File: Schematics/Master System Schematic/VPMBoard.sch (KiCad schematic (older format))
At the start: 23 parts

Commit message: VPMBoard Annotations
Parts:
- gave numbers to parts that had none: 23
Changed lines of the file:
@@
 > If car is charging, GLV_PreBRB\n will be driven by ChargerSupply12V\n\n> If car is not charging, GLV_PreBRB \nwill be disconnected from the \ncharger supply
 $Comp
-L power:GND #PWR?
+L power:GND #PWR01
 U 1 1 5FCA9C4C
 P 2050 1900
-F 0 "#PWR?" H 2050 1650 50  0001 C CNN
+F 0 "#PWR01" H 2050 1650 50  0001 C CNN
 F 1 "GND" H 2055 1727 50  0000 C CNN
 F 2 "" H 2050 1900 50  0001 C CNN
@@
 	2050 2400 1950 2400
 $Comp
-L power:GND #PWR?
+L power:GND #PWR02
 U 1 1 5FCC4D73
 P 2050 2550
-F 0 "#PWR?" H 2050 2300 50  0001 C CNN
+F 0 "#PWR02" H 2050 2300 50  0001 C CNN
 F 1 "GND" H 2055 2377 50  0000 C CNN
 F 2 "" H 2050 2550 50  0001 C CNN
@@
 ThermEXIn12V
 $Comp
-L power:GND #PWR?
+L power:GND #PWR012
 U 1 1 5FD5EF12
 P 8950 1900
-F 0 "#PWR?" H 8950 1650 50  0001 C CNN
+F 0 "#PWR012" H 8950 1650 50  0001 C CNN
 F 1 "GND" H 8955 1727 50  0000 C CNN
 F 2 "" H 8950 1900 50  0001 C CNN
@@
 $EndComp
 $Comp
-L Connector:Conn_01x02_Female J?
+L Connector:Conn_01x02_Female J20
 U 1 1 5FC6E9A5
 P 9600 1650
-F 0 "J?" H 9492 1325 50  0000 C CNN
+F 0 "J20" H 9492 1325 50  0000 C CNN
 F 1 "Therm_PWR" H 9500 1400 50  0000 C CNN
 F 2 "" H 9600 1650 50  0001 C CNN
@@
 $EndComp
 $Comp
-L Connector:Conn_01x04_Female J?
+L Connector:Conn_01x04_Female J14
 U 1 1 5FBD5D22
 P 1450 6050
-F 0 "J?" H 1342 5625 50  0000 C CNN
+F 0 "J14" H 1342 5625 50  0000 C CNN
 F 1 "GLV_Signal" H 1342 5716 50  0000 C CNN
 F 2 "" H 1450 6050 50  0001 C CNN
@@
 $EndComp
 $Comp
-L Connector:Conn_01x04_Female J?
+L Connector:Conn_01x04_Female J1
 U 1 1 5FC1125D
 P 1450 5400
-F 0 "J?" H 1342 4975 50  0000 C CNN
+F 0 "J1" H 1342 4975 50  0000 C CNN
 F 1 "Charge_Signal" H 1342 5066 50  0000 C CNN
 F 2 "" H 1450 5400 50  0001 C CNN
@@
 $EndComp
 $Comp
-L Connector:Conn_01x04_Female J?
+L Connector:Conn_01x04_Female J15
 U 1 1 5FC7CBDE
 P 1450 6700
-F 0 "J?" H 1342 6275 50  0000 C CNN
+F 0 "J15" H 1342 6275 50  0000 C CNN
 F 1 "Therm_Signal" H 1342 6366 50  0000 C CNN
 F 2 "" H 1450 6700 50  0001 C CNN
@@
 NoConn ~ 1650 6500
 $Comp
-L Connector:Conn_01x06_Female J?
+L Connector:Conn_01x06_Female J19
 U 1 1 5FDAC8DD
 P 4450 5950
-F 0 "J?" H 4342 5425 50  0000 C CNN
+F 0 "J19" H 4342 5425 50  0000 C CNN
 F 1 "BMS_Signal" H 4342 5516 50  0000 C CNN
 F 2 "" H 4450 5950 50  0001 C CNN
@@
 CANS_Chrg
 $Comp
-L power:GND #PWR?
+L power:GND #PWR04
 U 1 1 5FC9259C
 P 2850 6900
-F 0 "#PWR?" H 2850 6650 50  0001 C CNN
+F 0 "#PWR04" H 2850 6650 50  0001 C CNN
 F 1 "GND" H 2855 6727 50  0000 C CNN
 F 2 "" H 2850 6900 50  0001 C CNN
@@
 	4000 3550 4600 3550
 $Comp
-L Device:Q_PMOS_GDS Q?
+L Device:Q_PMOS_GDS Q2
 U 1 1 5FCC6DCE
 P 5350 3450
-F 0 "Q?" V 5599 3450 50  0000 C CNN
+F 0 "Q2" V 5599 3450 50  0000 C CNN
 F 1 "SQP50P03-07" V 5690 3450 50  0000 C CNN
 F 2 "" H 5550 3550 50  0001 C CNN
@@
 	5650 3550 5550 3550
 $Comp
-L Device:Fuse F?
+L Device:Fuse F200
 U 1 1 5FC0FA27
 P 4950 3550
-F 0 "F?" V 5147 3550 50  0000 C CNN
+F 0 "F200" V 5147 3550 50  0000 C CNN
 F 1 "12A" V 5056 3550 50  0000 C CNN
 F 2 "" V 4880 3550 50  0001 C CNN
@@
 	8250 3150 8300 3150
 $Comp
-L Device:Fuse F?
+L Device:Fuse F202
 U 1 1 5FB0792D
 P 8450 3250
-F 0 "F?" V 8647 3250 50  0000 C CNN
+F 0 "F202" V 8647 3250 50  0000 C CNN
 F 1 "1A" V 8556 3250 50  0000 C CNN
 F 2 "" V 8380 3250 50  0001 C CNN
@@
 $EndComp
 $Comp
-L Device:Fuse F?
+L Device:Fuse F201
 U 1 1 5FB100A8
 P 8450 3150
-F 0 "F?" V 8647 3150 50  0000 C CNN
+F 0 "F201" V 8647 3150 50  0000 C CNN
 F 1 "1A" V 8556 3150 50  0000 C CNN
 F 2 "" V 8380 3150 50  0001 C CNN
@@
 $EndComp
 $Comp
-L power:GND #PWR?
+L power:GND #PWR013
 U 1 1 5FCBC47D
 P 8950 3500
-F 0 "#PWR?" H 8950 3250 50  0001 C CNN
+F 0 "#PWR013" H 8950 3250 50  0001 C CNN
 F 1 "GND" H 8955 3327 50  0000 C CNN
 F 2 "" H 8950 3500 50  0001 C CNN
@@
 	7100 1550 7100 3250
 $Comp
-L Device:Q_PMOS_GDS Q?
+L Device:Q_PMOS_GDS Q6
 U 1 1 5FD075B5
 P 7450 3150
-F 0 "Q?" V 7699 3150 50  0000 C CNN
+F 0 "Q6" V 7699 3150 50  0000 C CNN
 F 1 "SQP50P03-07" V 7790 3150 50  0000 C CNN
 F 2 "" H 7650 3250 50  0001 C CNN
@@
 $EndComp
 $Comp
-L power:GND #PWR?
+L power:GND #PWR011
 U 1 1 5FD1386A
 P 8100 2800
-F 0 "#PWR?" H 8100 2550 50  0001 C CNN
+F 0 "#PWR011" H 8100 2550 50  0001 C CNN
 F 1 "GND" H 8105 2627 50  0000 C CNN
 F 2 "" H 8100 2800 50  0001 C CNN
@@
 	7450 2450 7450 2750
 $Comp
-L Device:R R?
+L Device:R R13
 U 1 1 5FD172BE
 P 7450 2300
-F 0 "R?" H 7520 2346 50  0000 L CNN
+F 0 "R13" H 7520 2346 50  0000 L CNN
 F 1 "100K" H 7520 2255 50  0000 L CNN
 F 2 "" V 7380 2300 50  0001 C CNN
@@
 $EndComp
 $Comp
-L power:+12V #PWR?
+L power:+12V #PWR05
 U 1 1 5FD2774A
 P 4600 3450
-F 0 "#PWR?" H 4600 3300 50  0001 C CNN
+F 0 "#PWR05" H 4600 3300 50  0001 C CNN
 F 1 "+12V" H 4615 3623 50  0000 C CNN
 F 2 "" H 4600 3450 50  0001 C CNN
@@
 	4600 3550 4800 3550
 $Comp
-L power:+12V #PWR?
+L power:+12V #PWR010
 U 1 1 5FD37608
 P 7450 2150
-F 0 "#PWR?" H 7450 2000 50  0001 C CNN
+F 0 "#PWR010" H 7450 2000 50  0001 C CNN
 F 1 "+12V" H 7465 2323 50  0000 C CNN
 F 2 "" H 7450 2150 50  0001 C CNN
@@
 GLV_BMSContainer\n
 $Comp
-L Transistor_FET:2N7002 Q?
+L Transistor_FET:2N7002 Q3
 U 1 1 5FCB5015
 P 5750 3000
-F 0 "Q?" V 5999 3000 50  0000 C CNN
+F 0 "Q3" V 5999 3000 50  0000 C CNN
 F 1 "2N7002" V 6090 3000 50  0000 C CNN
 F 2 "Package_TO_SOT_SMD:SOT-23" H 5950 2925 50  0001 L CIN
@@
 	4000 1550 6550 1550
 $Comp
-L Transistor_FET:2N7002 Q?
+L Transistor_FET:2N7002 Q4
 U 1 1 5FCCB41E
 P 6150 3000
-F 0 "Q?" V 6399 3000 50  0000 C CNN
+F 0 "Q4" V 6399 3000 50  0000 C CNN
 F 1 "2N7002" V 6490 3000 50  0000 C CNN
 F 2 "Package_TO_SOT_SMD:SOT-23" H 6350 2925 50  0001 L CIN
@@
 $EndComp
 $Comp
-L power:GND #PWR?
+L power:GND #PWR08
 U 1 1 5FCCC1B3
 P 6450 3200
-F 0 "#PWR?" H 6450 2950 50  0001 C CNN
+F 0 "#PWR08" H 6450 2950 50  0001 C CNN
 F 1 "GND" H 6455 3027 50  0000 C CNN
 F 2 "" H 6450 3200 50  0001 C CNN
@@
 	5350 3100 5350 3250
 $Comp
-L Device:R R?
+L Device:R R11
 U 1 1 5FCCFBA3
 P 5350 2850
-F 0 "R?" H 5420 2896 50  0000 L CNN
+F 0 "R11" H 5420 2896 50  0000 L CNN
 F 1 "100K" H 5420 2805 50  0000 L CNN
 F 2 "" V 5280 2850 50  0001 C CNN
@@
 $EndComp
 $Comp
-L power:+12V #PWR?
+L power:+12V #PWR06
 U 1 1 5FCD0144
 P 5350 2700
-F 0 "#PWR?" H 5350 2550 50  0001 C CNN
+F 0 "#PWR06" H 5350 2550 50  0001 C CNN
 F 1 "+12V" H 5365 2873 50  0000 C CNN
 F 2 "" H 5350 2700 50  0001 C CNN
@@
 Connection ~ 5750 1650
 $Comp
-L Transistor_FET:2N7002 Q?
+L Transistor_FET:2N7002 Q5
 U 1 1 5FCD3A37
 P 6550 2350
-F 0 "Q?" V 6799 2350 50  0000 C CNN
+F 0 "Q5" V 6799 2350 50  0000 C CNN
 F 1 "2N7002" V 6890 2350 50  0000 C CNN
 F 2 "Package_TO_SOT_SMD:SOT-23" H 6750 2275 50  0001 L CIN
@@
 $EndComp
 $Comp
-L power:GND #PWR?
+L power:GND #PWR09
 U 1 1 5FCD73FE
 P 6850 2550
-F 0 "#PWR?" H 6850 2300 50  0001 C CNN
+F 0 "#PWR09" H 6850 2300 50  0001 C CNN
 F 1 "GND" H 6855 2377 50  0000 C CNN
 F 2 "" H 6850 2550 50  0001 C CNN
@@
 	6550 1550 7100 1550
 $Comp
-L Device:R R?
+L Device:R R12
 U 1 1 5FCDD1F1
 P 6150 2150
-F 0 "R?" H 6220 2196 50  0000 L CNN
+F 0 "R12" H 6220 2196 50  0000 L CNN
 F 1 "100K" H 6220 2105 50  0000 L CNN
 F 2 "" V 6080 2150 50  0001 C CNN
@@
 $EndComp
 $Comp
-L power:+12V #PWR?
+L power:+12V #PWR07
 U 1 1 5FCDD6C3
 P 6150 2000
-F 0 "#PWR?" H 6150 1850 50  0001 C CNN
+F 0 "#PWR07" H 6150 1850 50  0001 C CNN
 F 1 "+12V" H 6165 2173 50  0000 C CNN
 F 2 "" H 6150 2000 50  0001 C CNN
@@
 	5750 1650 7800 1650
 $Comp
-L Transistor_FET:2N7002 Q?
+L Transistor_FET:2N7002 Q7
 U 1 1 5FCE3DFD
 P 7800 2650
-F 0 "Q?" V 8049 2650 50  0000 C CNN
+F 0 "Q7" V 8049 2650 50  0000 C CNN
 F 1 "2N7002" V 8140 2650 50  0000 C CNN
 F 2 "Package_TO_SOT_SMD:SOT-23" H 8000 2575 50  0001 L CIN
@@
 	2700 2550 2700 2400
 $Comp
-L power:GND #PWR?
+L power:GND #PWR03
 U 1 1 5FCAF3C3
 P 2700 2550
-F 0 "#PWR?" H 2700 2300 50  0001 C CNN
+F 0 "#PWR03" H 2700 2300 50  0001 C CNN
 F 1 "GND" H 2705 2377 50  0000 C CNN
 F 2 "" H 2700 2550 50  0001 C CNN
@@
 	3650 2300 3700 2300
 $Comp
-L Device:Q_NMOS_GDS Q?
+L Device:Q_NMOS_GDS Q1
 U 1 1 5FCA0094
 P 3900 2300
-F 0 "Q?" H 4104 2254 50  0000 L CNN
+F 0 "Q1" H 4104 2254 50  0000 L CNN
 F 1 "FDP3632" H 4104 2345 50  0000 L CNN
 F 2 "" H 4100 2400 50  0001 C CNN
@@
 $EndComp
 $Comp
-L Power_Management:LTC4357MS8 U?
+L Power_Management:LTC4357MS8 U5
 U 1 1 5FC9E54A
 P 3250 2400
-F 0 "U?" V 2850 1950 50  0000 C CNN
+F 0 "U5" V 2850 1950 50  0000 C CNN
 F 1 "LTC4357MS8" V 2950 2050 50  0000 C CNN
 F 2 "Package_SO:MSOP-8_3x3mm_P0.65mm" H 3500 2250 50  0001 L CNN
@@
 GLV_PreBRB
 $Comp
-L NER:2-Pos_Generic J?
+L NER:2-Pos_Generic J16
 U 1 1 60052B8B
 P 1500 3450
-F 0 "J?" H 1500 3575 50  0000 C CNN
+F 0 "J16" H 1500 3575 50  0000 C CNN
 F 1 "PumpIO" H 1500 3484 50  0000 C CNN
 F 2 "" H 1500 3450 50  0001 C CNN
@@
 	1250 3650 1200 3650
 $Comp
-L NER:3-Pos_Generic J?
+L NER:3-Pos_Generic J17
 U 1 1 60084A61
 P 1700 1450
-F 0 "J?" H 1700 1575 50  0000 C CNN
+F 0 "J17" H 1700 1575 50  0000 C CNN
 F 1 "GLV/Charge_PWR" H 1700 1484 50  0000 C CNN
 F 2 "" H 1700 1450 50  0001 C CNN
@@
 	1450 1550 1400 1550
 $Comp
-L NER:1-Pos_Generic J?
+L NER:1-Pos_Generic J18
 U 1 1 600B3510
 P 1700 2300
-F 0 "J?" H 1700 2425 50  0000 C CNN
+F 0 "J18" H 1700 2425 50  0000 C CNN
 F 1 "GND_QC" H 1700 2334 50  0000 C CNN
 F 2 "" H 1700 2300 50  0001 C CNN
@@
 	1450 1750 1400 1750
 $Comp
-L NER:3-Pos_Generic J?
+L NER:3-Pos_Generic J21
 U 1 1 6116408D
 P 9650 3050
-F 0 "J?" H 9650 3175 50  0000 C CNN
+F 0 "J21" H 9650 3175 50  0000 C CNN
 F 1 "BMS_PWR" H 9650 3084 50  0000 C CNN
 F 2 "" H 9650 3050 50  0001 C CNN

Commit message: Added/Fixed Sheet Connections Within BMS Container
> Added hierarchical labels for each input on the VPM and connected them to hierarchical labels and the BMS within the BMS container.
> Added CANS(Charger) hierarchical label coming out of the BMS container sheet and connected it to the charger CAN bus line.

BMS Container Version 8.1
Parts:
- removed J1: Charge_Signal, symbol Connector:Conn_01x04_Female
- removed J14: GLV_Signal, symbol Connector:Conn_01x04_Female
- removed J15: Therm_Signal, symbol Connector:Conn_01x04_Female
- removed J19: BMS_Signal, symbol Connector:Conn_01x06_Female
- removed J20: Therm_PWR, symbol Connector:Conn_01x02_Female
- added J1: Charge_Signal, symbol NER:4-Pos_Generic
- added J14: Main_Signal, symbol NER:4-Pos_Generic
- added J15: Therm_Signal, symbol NER:4-Pos_Generic
- added J19: BMS_Signal, symbol NER:6-Pos_Generic
- added J20: ThermEX_PWR, symbol NER:2-Pos_Generic
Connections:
- net labels added: BMS_Fault, CANH_BMS, CANH_Chrg, CANH_Main, CANH_Thrm, CANL_BMS, CANL_Chrg, CANL_Main, CANL_Thrm, CANS_BMS, CANS_Chrg, CANS_Main, CANS_Thrm, Charge_Safety, ChargerSafety, MP_EN, ThermEX_GND, ThermEX_PWR
- net labels removed: ???
- no-connect marks 2 -> 4
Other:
- note added: "ThermEX_PWR\n"
- note removed: "ThermEXIn12V"
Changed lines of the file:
@@
 EESchema Schematic File Version 4
-LIBS:Master System Schematic-cache
 EELAYER 30 0
 EELAYER END
@@
 	8950 1900 8950 1750
 Connection ~ 8250 1650
-Text Notes 9350 1650 2    50   ~ 0
-ThermEXIn12V
 $Comp
 L power:GND #PWR012
@@
 	-1   0    0    -1
 $EndComp
-$Comp
-L Connector:Conn_01x02_Female J20
-U 1 1 5FC6E9A5
-P 9600 1650
-F 0 "J20" H 9492 1325 50  0000 C CNN
-F 1 "Therm_PWR" H 9500 1400 50  0000 C CNN
-F 2 "" H 9600 1650 50  0001 C CNN
-F 3 "~" H 9600 1650 50  0001 C CNN
-	1    9600 1650
-	1    0    0    -1
-$EndComp
-$Comp
-L Connector:Conn_01x04_Female J14
-U 1 1 5FBD5D22
-P 1450 6050
-F 0 "J14" H 1342 5625 50  0000 C CNN
-F 1 "GLV_Signal" H 1342 5716 50  0000 C CNN
-F 2 "" H 1450 6050 50  0001 C CNN
-F 3 "~" H 1450 6050 50  0001 C CNN
-	1    1450 6050
-	-1   0    0    1
-$EndComp
-$Comp
-L Connector:Conn_01x04_Female J1
-U 1 1 5FC1125D
-P 1450 5400
-F 0 "J1" H 1342 4975 50  0000 C CNN
-F 1 "Charge_Signal" H 1342 5066 50  0000 C CNN
-F 2 "" H 1450 5400 50  0001 C CNN
-F 3 "~" H 1450 5400 50  0001 C CNN
-	1    1450 5400
-	-1   0    0    1
-$EndComp
-$Comp
-L Connector:Conn_01x04_Female J15
-U 1 1 5FC7CBDE
-P 1450 6700
-F 0 "J15" H 1342 6275 50  0000 C CNN
-F 1 "Therm_Signal" H 1342 6366 50  0000 C CNN
-F 2 "" H 1450 6700 50  0001 C CNN
-F 3 "~" H 1450 6700 50  0001 C CNN
-	1    1450 6700
-	-1   0    0    1
-$EndComp
 NoConn ~ 1650 6500
-$Comp
-L Connector:Conn_01x06_Female J19
-U 1 1 5FDAC8DD
-P 4450 5950
-F 0 "J19" H 4342 5425 50  0000 C CNN
-F 1 "BMS_Signal" H 4342 5516 50  0000 C CNN
-F 2 "" H 4450 5950 50  0001 C CNN
-F 3 "~" H 4450 5950 50  0001 C CNN
-	1    4450 5950
-	1    0    0    1
-$EndComp
 Wire Wire Line
 	1650 5950 3050 5950
@@
 F 3 "" H 1700 2300 50  0001 C CNN
 	1    1700 2300
-	1    0    0    -1
+	-1   0    0    -1
 $EndComp
 Text HLabel 1400 1750 0    50   UnSpc ~ 0
@@
 PWR_Ready
 Text HLabel 9950 3350 2    50   Output ~ 0
-???
+BMS_GND
 Wire Wire Line
 	9950 3350 9900 3350
@@
 Wire Wire Line
 	9950 3150 9900 3150
+$Comp
+L NER:2-Pos_Generic J20
+U 1 1 600B417F
+P 9650 1550
+F 0 "J20" H 9650 1675 50  0000 C CNN
+F 1 "ThermEX_PWR" H 9650 1584 50  0000 C CNN
+F 2 "" H 9650 1550 50  0001 C CNN
+F 3 "" H 9650 1550 50  0001 C CNN
+	1    9650 1550
+	1    0    0    -1
+$EndComp
+Text HLabel 9900 1750 2    50   Output ~ 0
+ThermEX_GND
+Text HLabel 9900 1650 2    50   Output ~ 0
+ThermEX_PWR
+Text Notes 9350 1650 2    50   ~ 0
+ThermEX_PWR\n
+$Comp
+L NER:4-Pos_Generic J14
+U 1 1 600E1D3A
+P 1400 5750
+F 0 "J14" H 1400 5875 50  0000 C CNN
+F 1 "Main_Signal" H 1400 5784 50  0000 C CNN
+F 2 "" H 1400 5750 50  0001 C CNN
+F 3 "" H 1400 5750 50  0001 C CNN
+	1    1400 5750
+	-1   0    0    -1
+$EndComp
+$Comp
+L NER:4-Pos_Generic J15
+U 1 1 600E4AAA
+P 1400 6400
+F 0 "J15" H 1400 6525 50  0000 C CNN
+F 1 "Therm_Signal" H 1400 6434 50  0000 C CNN
+F 2 "" H 1400 6400 50  0001 C CNN
+F 3 "" H 1400 6400 50  0001 C CNN
+	1    1400 6400
+	-1   0    0    -1
+$EndComp
+NoConn ~ 1150 6500
+Text HLabel 1150 5500 0    50   Input ~ 0
+CANS_Chrg
+Text HLabel 1150 5400 0    50   Input ~ 0
+CANL_Chrg
+Text HLabel 1150 5300 0    50   Input ~ 0
+CANH_Chrg
+Text HLabel 1150 5200 0    50   Input ~ 0
+ChargerSafety
+Text HLabel 1150 6150 0    50   Input ~ 0
+CANS_Main
+Text HLabel 1150 6050 0    50   Input ~ 0
+CANL_Main
+Text HLabel 1150 5950 0    50   Input ~ 0
+CANH_Main
+Text HLabel 1150 5850 0    50   Input ~ 0
+BMS_Fault
+Text HLabel 1150 6800 0    50   Input ~ 0
+CANS_Thrm
+Text HLabel 1150 6600 0    50   Input ~ 0
+CANH_Thrm
+Text HLabel 1150 6700 0    50   Input ~ 0
+CANL_Thrm
+$Comp
+L NER:6-Pos_Generic J19
+U 1 1 600F4343
+P 4500 5550
+F 0 "J19" H 4500 5675 50  0000 C CNN
+F 1 "BMS_Signal" H 4500 5584 50  0000 C CNN
+F 2 "" H 4500 5550 50  0001 C CNN
+F 3 "" H 4500 5550 50  0001 C CNN
+	1    4500 5550
+	1    0    0    -1
+$EndComp
+$Comp
+L NER:4-Pos_Generic J1
+U 1 1 600D5093
+P 1400 5100
+F 0 "J1" H 1400 5225 50  0000 C CNN
+F 1 "Charge_Signal" H 1400 5134 50  0000 C CNN
+F 2 "" H 1400 5100 50  0001 C CNN
+F 3 "" H 1400 5100 50  0001 C CNN
+	1    1400 5100
+	-1   0    0    -1
+$EndComp
+NoConn ~ 4750 5650
+Text HLabel 4750 5750 2    50   Input ~ 0
+Charge_Safety
+Text HLabel 4750 5850 2    50   Input ~ 0
+MP_EN
+Text HLabel 4750 5950 2    50   Input ~ 0
+CANH_BMS
+Text HLabel 4750 6050 2    50   Input ~ 0
+CANL_BMS
+Text HLabel 4750 6150 2    50   Input ~ 0
+CANS_BMS
 $EndSCHEMATC

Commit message: Moved Pump power fuse to branching point
moved to GLVMS
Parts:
- removed F200: 12A, symbol Device:Fuse
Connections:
- net +12V: now also Q2.3 (S)
- new net: J1.1, J19.2
- new net: J1.2, J14.2, J15.2, J19.4
- new net: J1.3, J14.3, J15.3, J19.5
- new net: J14.1, J19.3
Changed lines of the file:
@@
 	1650 5850 4250 5850
 NoConn ~ 4250 5650
-Wire Wire Line
-	5100 3550 5150 3550
-Wire Wire Line
-	4000 3550 4600 3550
 $Comp
 L Device:Q_PMOS_GDS Q2
@@
 Wire Wire Line
 	5650 3550 5550 3550
-$Comp
-L Device:Fuse F200
-U 1 1 5FC0FA27
-P 4950 3550
-F 0 "F200" V 5147 3550 50  0000 C CNN
-F 1 "12A" V 5056 3550 50  0000 C CNN
-F 2 "" V 4880 3550 50  0001 C CNN
-F 3 "~" H 4950 3550 50  0001 C CNN
-	1    4950 3550
-	0    -1   -1   0
-$EndComp
 Wire Wire Line
 	8250 1650 8250 3150
@@
 	1    0    0    -1
 $EndComp
-Wire Wire Line
-	4600 3450 4600 3550
-Connection ~ 4600 3550
-Wire Wire Line
-	4600 3550 4800 3550
 $Comp
 L power:+12V #PWR010
@@
 Text HLabel 4750 6150 2    50   Input ~ 0
 CANS_BMS
+Wire Wire Line
+	4000 3550 4600 3550
+Wire Wire Line
+	4600 3450 4600 3550
+Connection ~ 4600 3550
+Wire Wire Line
+	4600 3550 5150 3550
 $EndSCHEMATC

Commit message: Annotation and Revision numbers
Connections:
- new net: J1.1, J19.2
- new net: J1.2, J14.2, J15.2, J19.4
- new net: J1.3, J14.3, J15.3, J19.5
- new net: J14.1, J19.3
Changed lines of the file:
@@
 Sheet 22 23
 Title "Vehicle Power Management Board"
-Date "2020-12-05"
-Rev "4.1"
+Date "2021-01-30"
+Rev "4.2"
 Comp "Northeastern Electric Racing"
 Comment1 "https://github.com/Northeastern-Electric-Racing/NER"

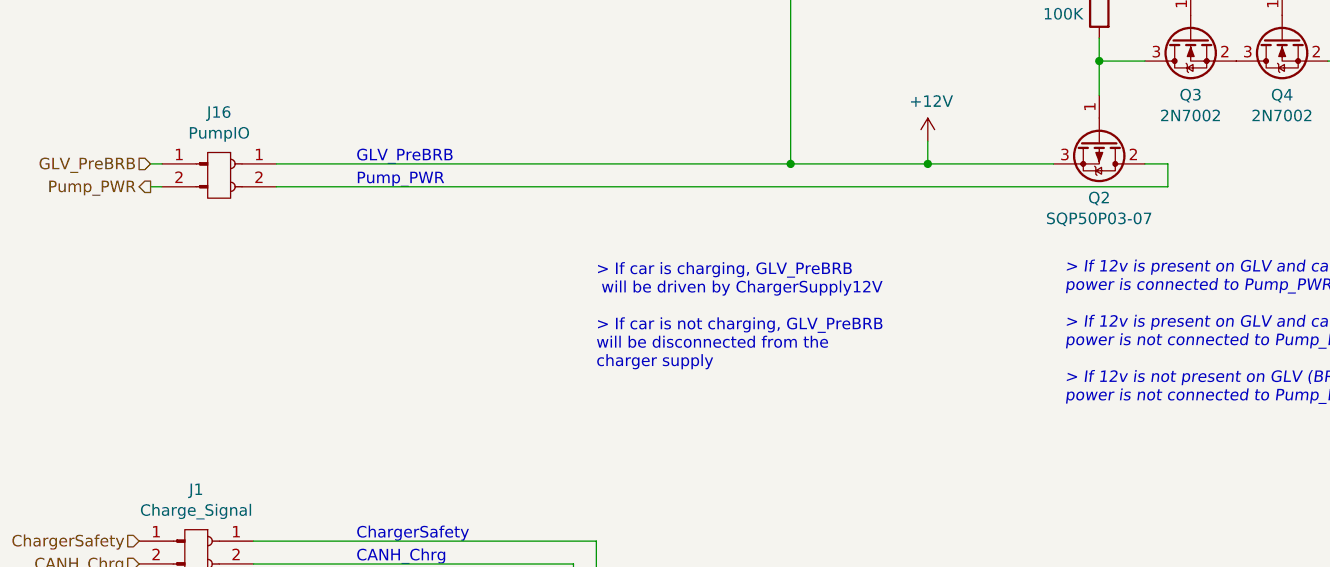
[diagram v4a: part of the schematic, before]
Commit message: VPM Board Flyback Diode
> Added MBRD5100 diode for protection against voltage spikes when switching the motor.
> Added note explaining this ^

VPM Board Version 4.3
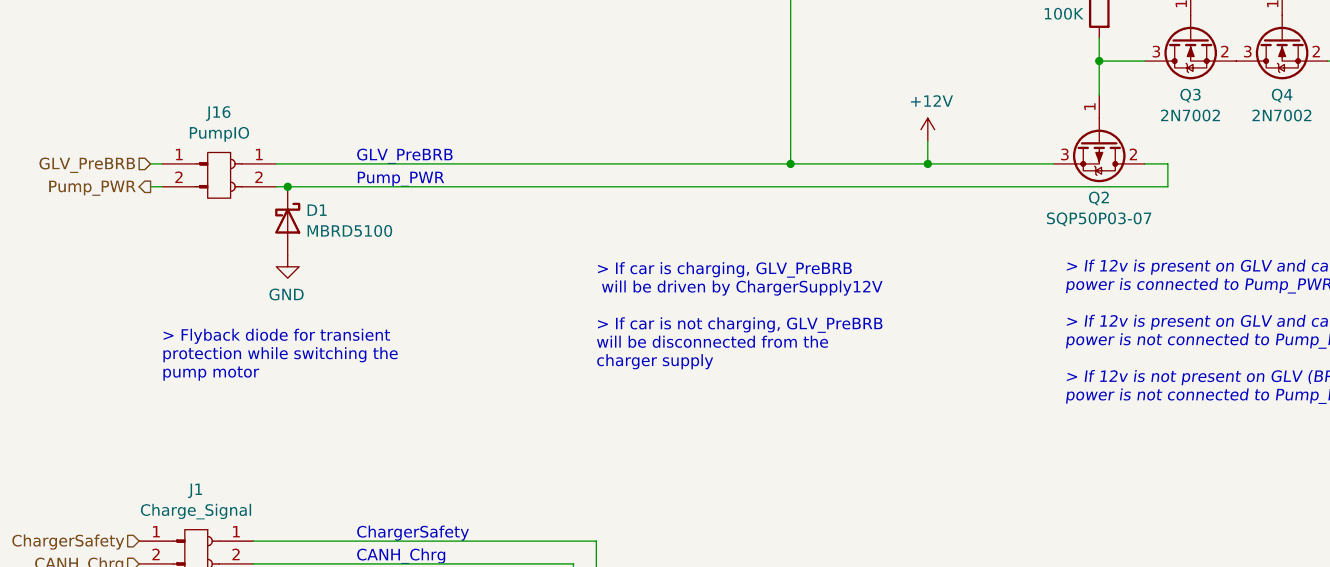
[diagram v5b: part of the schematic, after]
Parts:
- added D1: MBRD5100, Diode_SMD:D_SOD-123, symbol Diode:MBR0520
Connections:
- net GND: now also D1.2 (A)
- net at J16.2, Q2.2 (D): now also D1.1 (K)
- new net: J1.1, J19.2
- new net: J1.2, J14.2, J15.2, J19.4
- new net: J1.3, J14.3, J15.3, J19.5
- new net: J14.1, J19.3
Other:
- note added: "> Flyback diode for transient\nprotection while switching the \npump motor"
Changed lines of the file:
@@
 Sheet 22 23
 Title "Vehicle Power Management Board"
-Date "2021-01-30"
-Rev "4.2"
+Date "2021-02-11"
+Rev "4.3"
 Comp "Northeastern Electric Racing"
 Comment1 "https://github.com/Northeastern-Electric-Racing/NER"
@@
 	1750 3550 4000 3550
 Wire Wire Line
-	1750 3650 5650 3650
+	1750 3650 1800 3650
 Wire Wire Line
 	1250 3550 1200 3550
@@
 Wire Wire Line
 	4600 3550 5150 3550
+$Comp
+L Diode:MBR0520 D1
+U 1 1 602AC2AA
+P 1800 3800
+F 0 "D1" V 1754 3880 50  0000 L CNN
+F 1 "MBRD5100" V 1845 3880 50  0000 L CNN
+F 2 "Diode_SMD:D_SOD-123" H 1800 3625 50  0001 C CNN
+F 3 "http://www.mccsemi.com/up_pdf/MBR0520~MBR0580(SOD123).pdf" H 1800 3800 50  0001 C CNN
+	1    1800 3800
+	0    1    1    0
+$EndComp
+$Comp
+L power:GND #PWR014
+U 1 1 602ADBC9
+P 1800 3950
+F 0 "#PWR014" H 1800 3700 50  0001 C CNN
+F 1 "GND" H 1805 3777 50  0000 C CNN
+F 2 "" H 1800 3950 50  0001 C CNN
+F 3 "" H 1800 3950 50  0001 C CNN
+	1    1800 3950
+	-1   0    0    -1
+$EndComp
+Text Notes 1250 4500 0    50   ~ 0
+> Flyback diode for transient\nprotection while switching the \npump motor
+Connection ~ 1800 3650
+Wire Wire Line
+	1800 3650 5650 3650
 $EndSCHEMATC

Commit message: Revert "Revert "Merge branch 'Dylan_BMS-control-systems-slight-rework' of https://github.com/Northeastern-Electric-Racing/NER into Dylan_BMS-control-systems-slight-rework""
This reverts commit 7bfceb9de4e286d5e46c7b991145f3115c617458.
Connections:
- new net: J1.1, J19.2
- new net: J1.2, J14.2, J15.2, J19.4
- new net: J1.3, J14.3, J15.3, J19.5
- new net: J14.1, J19.3
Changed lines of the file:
@@
 $Descr A 11000 8500
 encoding utf-8
-Sheet 22 23
+Sheet 23 23
 Title "Vehicle Power Management Board"
 Date "2021-02-11"

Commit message: Revert "Merge branch 'Dylan_BMS-control-systems-slight-rework' of https://github.com/Northeastern-Electric-Racing/NER into Dylan_BMS-control-systems-slight-rework"
This reverts commit fde7ba4e4a38cad13224d6abfd117b52e4ba179f, reversing
changes made to 479d55be7c023c6502d2d4db07d9957a4b0a3a94.
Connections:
- new net: J1.1, J19.2
- new net: J1.2, J14.2, J15.2, J19.4
- new net: J1.3, J14.3, J15.3, J19.5
- new net: J14.1, J19.3
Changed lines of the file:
@@
 $Descr A 11000 8500
 encoding utf-8
-Sheet 23 23
+Sheet 22 23
 Title "Vehicle Power Management Board"
 Date "2021-02-11"
